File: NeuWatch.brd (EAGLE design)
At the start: 43.2 x 40.6 mm, 68 parts, among them IC1 SAMD21G18A-AUT, IC3 TPS2115, IC4 SIP32401A, IC5 MC74VHC1G14DFT, T1 846, T2 2N7002_ALT, Y1 32,768Khz

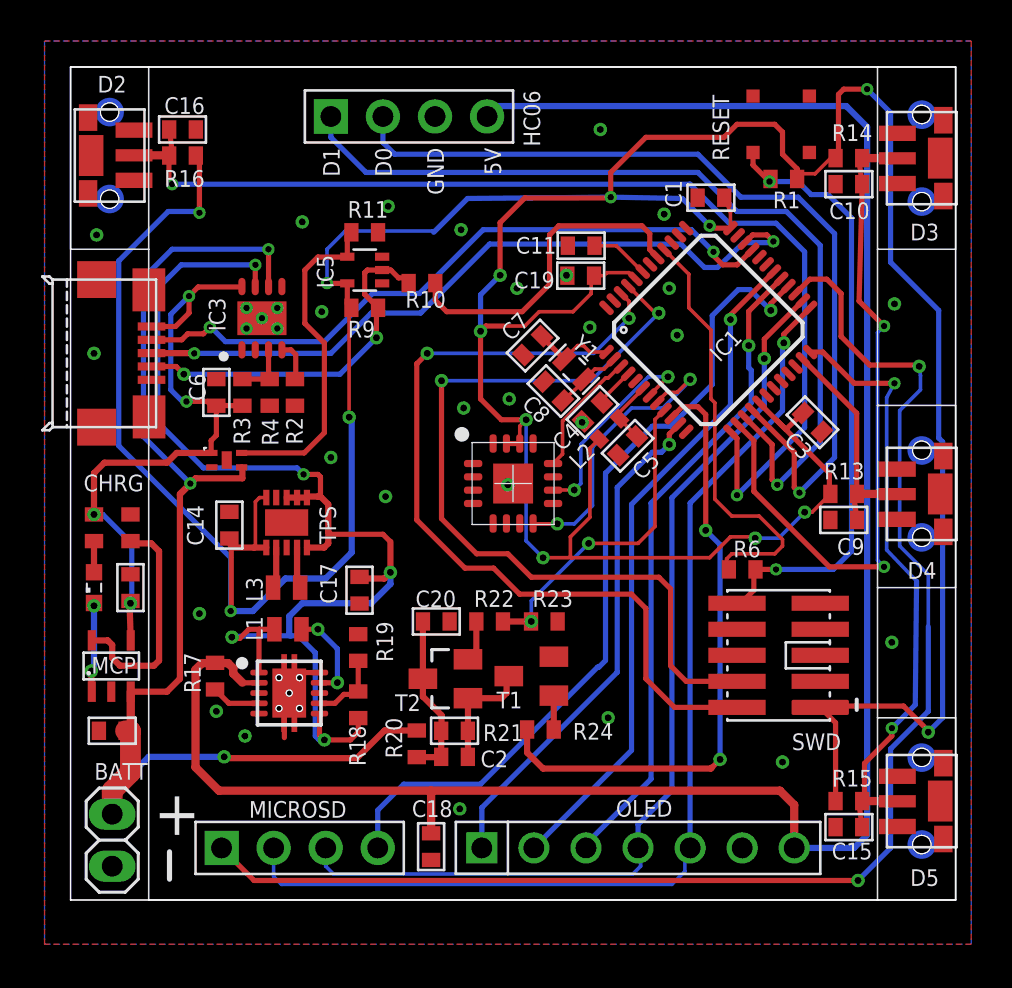
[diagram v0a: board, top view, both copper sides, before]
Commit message: removed boost and others
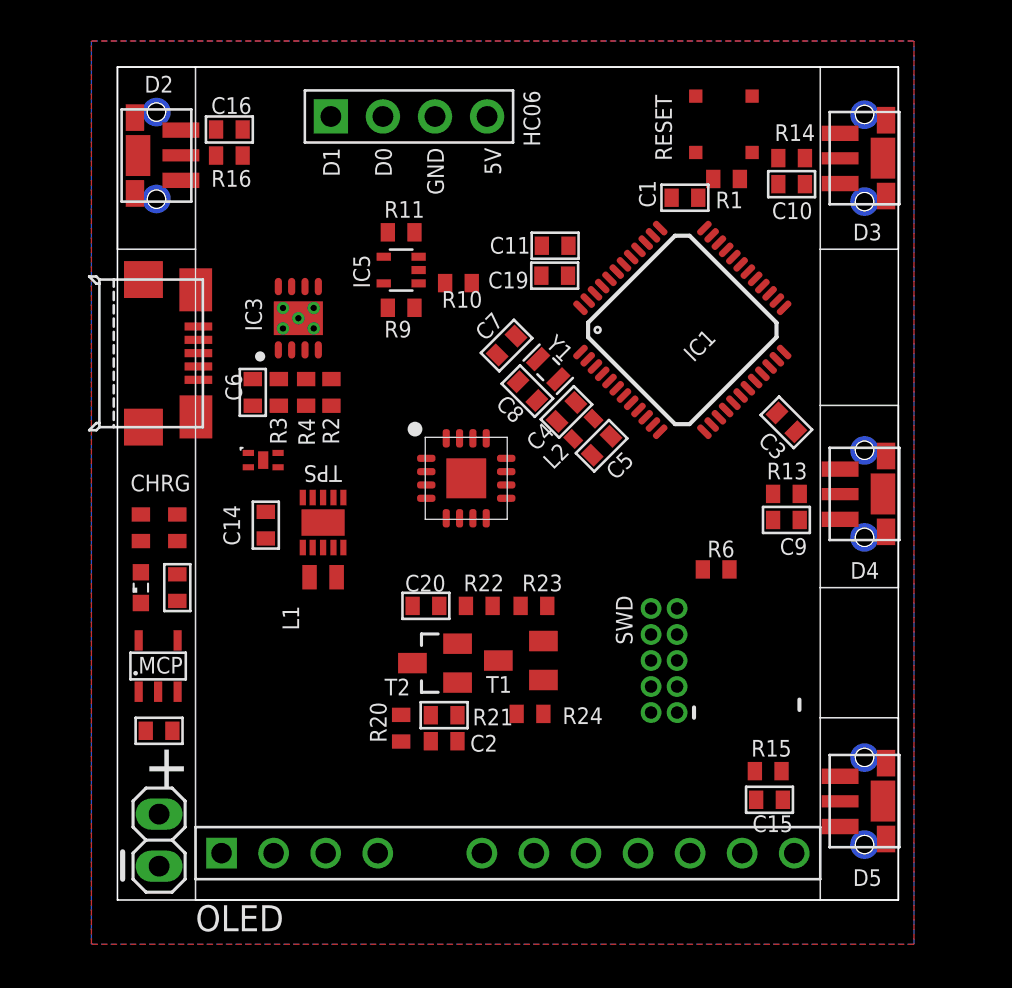
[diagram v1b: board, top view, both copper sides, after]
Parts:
- removed BOOST: TPS6102X, AtomTech:DRC
- removed C17: 10 uF, AtomTech:C0402
- removed C18: 47uf, AtomTech:C0402
- removed L3: 6.8 uH, Bourns_By_element14_Batch_1:INDC1610X12N
- removed MICROSD: 1X4, AtomTech:1B4
- removed R17, R18, R19: 100K, adafruit:R0402
- OLED: value 1X7 -> 1.5-OLED; device AtomTech:1X7 -> AtomTech:1.5OLED
- SWD: value SWD -> PINHEAD-2x5-P1.27; device AtomTech:PARTS_CC-P05 -> Neutrino-:ARDUINO-NEUTRINO-082_CONNETTORI_PINHEAD-2X5-P127
- moved OLED 12.7 mm to (7.49, 2.29)
- moved SWD 5.59 mm to (29.1, 11.7), turned to 180 degrees
- moved R15 4.20 mm to (34.2, 6.29)
- moved C15 4.10 mm to (34.2, 4.89)
- moved C10 2.79 mm to (35.3, 34.9)
- moved R14 2.79 mm to (35.3, 36.2)
- moved RESET 2.79 mm to (32.0, 37.8)
- moved C9 2.79 mm to (35.1, 18.5)
- moved D3 2.79 mm to (38.9, 36.2)
- moved D4 2.79 mm to (38.9, 19.8)
- moved D5 2.79 mm to (38.9, 4.83)
- moved R1 2.79 mm to (32.1, 35.2)
- moved R13 2.79 mm to (35.1, 19.8)
- moved U$1 2.30 mm to (19.4, 20.6)
- moved BATT 2.29 mm to (4.45, 2.92)
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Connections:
- removed net 5V: BOOST.2, C18.1, HC06.P$4, OLED.P$7, R17.2
- removed net LBI: BOOST.7, R18.1, R19.2
- removed net LBO: BOOST.4, R17.1
- removed net SW: BOOST.9, L3.2
- net D6: now also OLED.P$9; no longer OLED.P$3
- net D7: now also OLED.P$5; no longer OLED.P$2
- net D8: now also OLED.P$6; no longer OLED.P$1
- net GND: now also OLED.P$10; no longer BOOST.10, BOOST.5, BOOST.8, BOOST.EXP, C17.2, C18.2, OLED.P$6, R19.1
- net MISO/D12: now also OLED.P$4; no longer MICROSD.P$4
- net MOSI/D11: now also OLED.P$2, OLED.P$7; no longer MICROSD.P$2, OLED.P$5
- net SCK/D13: now also OLED.P$3, OLED.P$8; no longer MICROSD.P$3, OLED.P$4
- net SS/D10: now also OLED.P$1; no longer MICROSD.P$1
- net VIN: now also HC06.P$4, OLED.P$11
- net VMAIN: no longer BOOST.1, BOOST.6, C17.1, L3.1, R18.2
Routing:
- net 3.3V: track 211.1 -> 0.00 mm, vias 14 -> 0
- net 5V: track 100.2 -> 0.00 mm
- net SS/D10: track 68.5 -> 0.00 mm, vias 2 -> 0
- net VIN: track 59.8 -> 0.00 mm, vias 3 -> 0
- net VMAIN: track 58.9 -> 0.00 mm, vias 5 -> 0
- net D2: track 53.2 -> 0.00 mm, vias 2 -> 0
- net MOSI/D11: track 51.9 -> 0.00 mm, vias 1 -> 0
- net SCK/D13: track 47.5 -> 0.00 mm, vias 1 -> 0
- net D1: track 43.6 -> 0.00 mm, vias 1 -> 0
- net D0: track 43.5 -> 0.00 mm, vias 1 -> 0
- net PA31_SWDIO: track 41.7 -> 0.00 mm, vias 2 -> 0
- net MISO/D12: track 40.8 -> 0.00 mm, vias 1 -> 0
- net PA30_SWCLK: track 40.6 -> 0.00 mm, vias 2 -> 0
- net TARGET_USB_P: track 35.2 -> 0.00 mm, vias 2 -> 0
- net D3: track 34.0 -> 0.00 mm, vias 2 -> 0
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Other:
- board size 43.2 x 40.6 mm -> 38.1 x 40.6 mm

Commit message: pinout fixed
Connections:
- net D6: now also OLED.P$5; no longer OLED.P$9
- net D7: now also OLED.P$6; no longer OLED.P$5
- net D8: now also OLED.P$7; no longer OLED.P$6
- net MOSI/D11: now also OLED.P$9; no longer OLED.P$7
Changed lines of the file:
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@@
 <signal name="MOSI/D11">
 <contactref element="IC1" pad="25"/>
-<contactref element="OLED" pad="P$7"/>
+<contactref element="OLED" pad="P$9"/>
 <contactref element="OLED" pad="P$2"/>
-<wire x1="25.273" y1="2.286" x2="34.939425" y2="28.8913375" width="0" layer="19" extent="1-1"/>
-<wire x1="10.033" y1="2.286" x2="25.273" y2="2.286" width="0" layer="19" extent="1-1"/>
+<wire x1="30.353" y1="2.286" x2="34.939425" y2="28.8913375" width="0" layer="19" extent="1-1"/>
+<wire x1="10.033" y1="2.286" x2="30.353" y2="2.286" width="0" layer="19" extent="1-1"/>
 </signal>
 <signal name="SS/D10">
@@
 <signal name="D6">
 <contactref element="IC1" pad="29"/>
-<contactref element="OLED" pad="P$9"/>
-<wire x1="30.353" y1="2.286" x2="33.525209375" y2="30.30555" width="0" layer="19" extent="1-1"/>
+<contactref element="OLED" pad="P$5"/>
+<wire x1="20.193" y1="2.286" x2="33.525209375" y2="30.30555" width="0" layer="19" extent="1-1"/>
 </signal>
 <signal name="TARGET_USB_N">
@@
 <signal name="D7">
 <contactref element="IC1" pad="30"/>
-<contactref element="OLED" pad="P$5"/>
-<wire x1="20.193" y1="2.286" x2="33.17165625" y2="30.659103125" width="0" layer="19" extent="1-1"/>
+<contactref element="OLED" pad="P$6"/>
+<wire x1="22.733" y1="2.286" x2="33.17165625" y2="30.659103125" width="0" layer="19" extent="1-1"/>
 </signal>
 <signal name="D8">
 <contactref element="IC1" pad="11"/>
-<contactref element="OLED" pad="P$6"/>
-<wire x1="22.733" y1="2.286" x2="28.54010625" y2="23.199128125" width="0" layer="19" extent="1-1"/>
+<contactref element="OLED" pad="P$7"/>
+<wire x1="25.273" y1="2.286" x2="28.54010625" y2="23.199128125" width="0" layer="19" extent="1-1"/>
 </signal>
 <signal name="D9">

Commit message: high side load
for OLED and UART cutoff
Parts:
- added C17, C18: 470nf, AtomTech:C0402
- added R7: 10, rcl:R0402
- added R8: 4.7k, rcl:R0402
- added U$3: AAT4610B, AtomTech:SOT23-5
- moved C20 3.64 mm to (21.0, 13.6)
- moved R20 3.64 mm to (19.8, 7.62)
- moved R22 3.64 mm to (23.6, 13.6)
- moved R23 3.64 mm to (26.3, 13.6)
- moved R24 3.64 mm to (26.1, 8.32)
- moved T1 3.64 mm to (25.7, 10.9)
- moved T2 3.64 mm to (21.5, 10.8)
- moved C2 3.64 mm to (21.9, 8.26)
- moved R21 3.64 mm to (21.9, 6.99)
- moved SWD 3.30 mm to (32.4, 11.8)
- moved R6 0.77 mm to (31.8, 16.9), turned to 270 degrees
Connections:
- new net N$10: R7.2, U$3.4
- new net N$11: R8.2, U$3.3
- new net VCBATT: C17.1, HC06.P$4, OLED.P$11, U$3.1
- net D9: now also R7.1
- net GND: now also C17.2, C18.2, R8.1, U$3.2
- net VIN: now also C18.1, U$3.5; no longer HC06.P$4, OLED.P$11

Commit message: fixes
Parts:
- L1: value 1.5 uH -> 120 nH
- RESET: device parts:PTS540 -> AtomTech:PTS540
- moved R10 10.3 mm to (9.14, 33.0), turned to 180 degrees
- moved R7 7.38 mm to (8.26, 12.6), turned to 270 degrees
- moved R11 7.22 mm to (9.14, 31.3), turned to 0 degrees
- moved R1 6.77 mm to (25.9, 37.8), turned to 90 degrees
- moved IC4 6.37 mm to (9.02, 15.1)
- moved R8 5.67 mm to (10.9, 12.6), turned to 270 degrees
- moved IC5 4.78 mm to (11.7, 32.1), turned to 180 degrees
- moved C17 4.56 mm to (11.0, 5.71), turned to 270 degrees
- moved R9 4.16 mm to (13.7, 32.1), turned to 270 degrees
- moved U$1 2.05 mm to (21.5, 20.3)
- moved RESET 1.90 mm to (30.1, 37.8)
- moved U$3 1.78 mm to (10.9, 9.27), turned to 90 degrees
- moved C18 1.42 mm to (8.51, 5.71), turned to 270 degrees
- moved C6 1.20 mm to (8.64, 23.6)
- moved IC3 1.20 mm to (10.9, 27.2)
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
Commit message: redesign
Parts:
- moved RESET 26.8 mm to (38.1, 12.3), turned to 270 degrees
- moved R1 22.7 mm to (33.3, 16.4), turned to 0 degrees
- moved R23 11.0 mm to (15.4, 12.3), turned to 270 degrees
- moved R22 9.15 mm to (15.4, 9.65), turned to 270 degrees
- moved C20 8.64 mm to (15.4, 7.05), turned to 90 degrees
- moved T1 7.66 mm to (18.0, 11.7), turned to 180 degrees
- moved R24 6.66 mm to (20.6, 12.1), turned to 270 degrees
- moved T2 4.67 mm to (18.2, 7.49), turned to 180 degrees
- moved C11 2.73 mm to (25.6, 33.9), turned to 135 degrees
- moved C19 2.51 mm to (24.6, 32.8), turned to 135 degrees
- moved R20 2.34 mm to (21.3, 5.84), turned to 180 degrees
- moved C9 2.05 mm to (35.8, 20.4), turned to 90 degrees
- moved C10 1.94 mm to (35.7, 36.8), turned to 90 degrees
- moved C6 1.78 mm to (10.4, 23.7)
- moved IC3 1.78 mm to (12.6, 27.4)
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
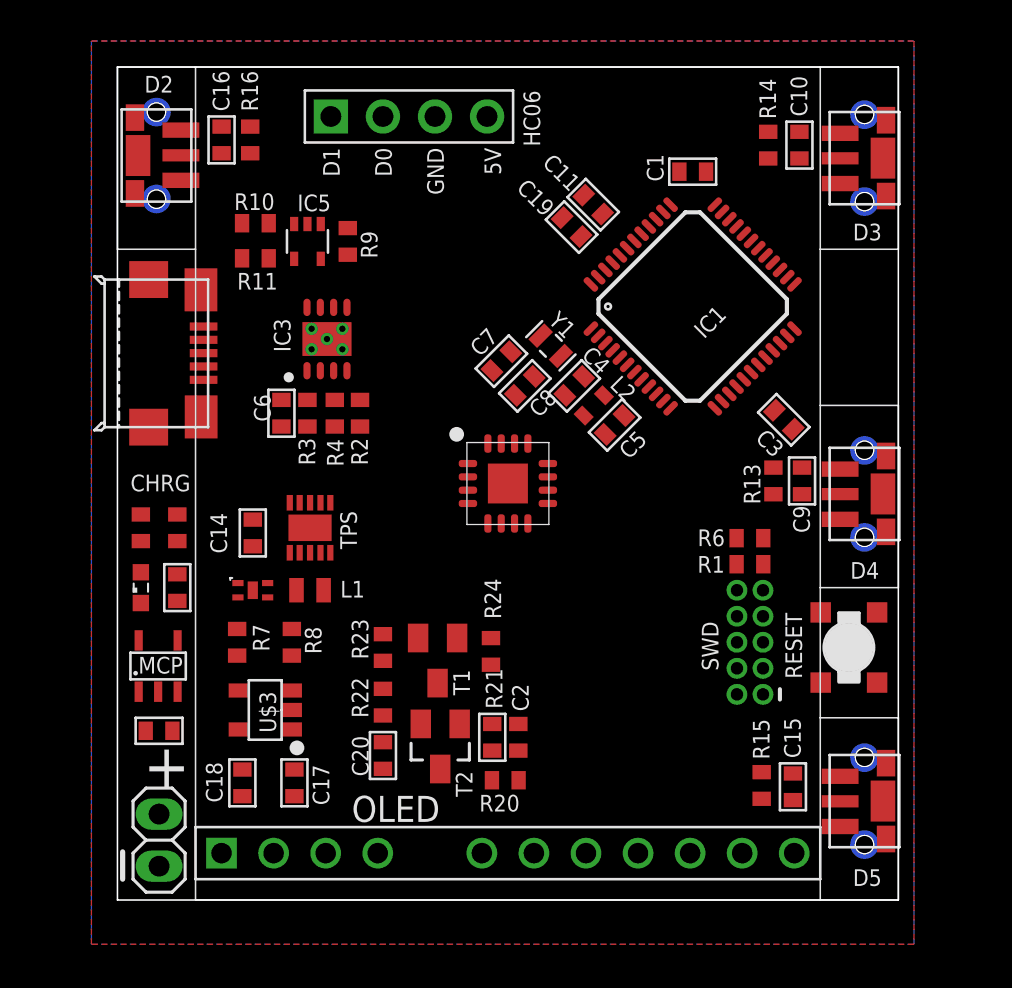
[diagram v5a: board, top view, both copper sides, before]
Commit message: vin control
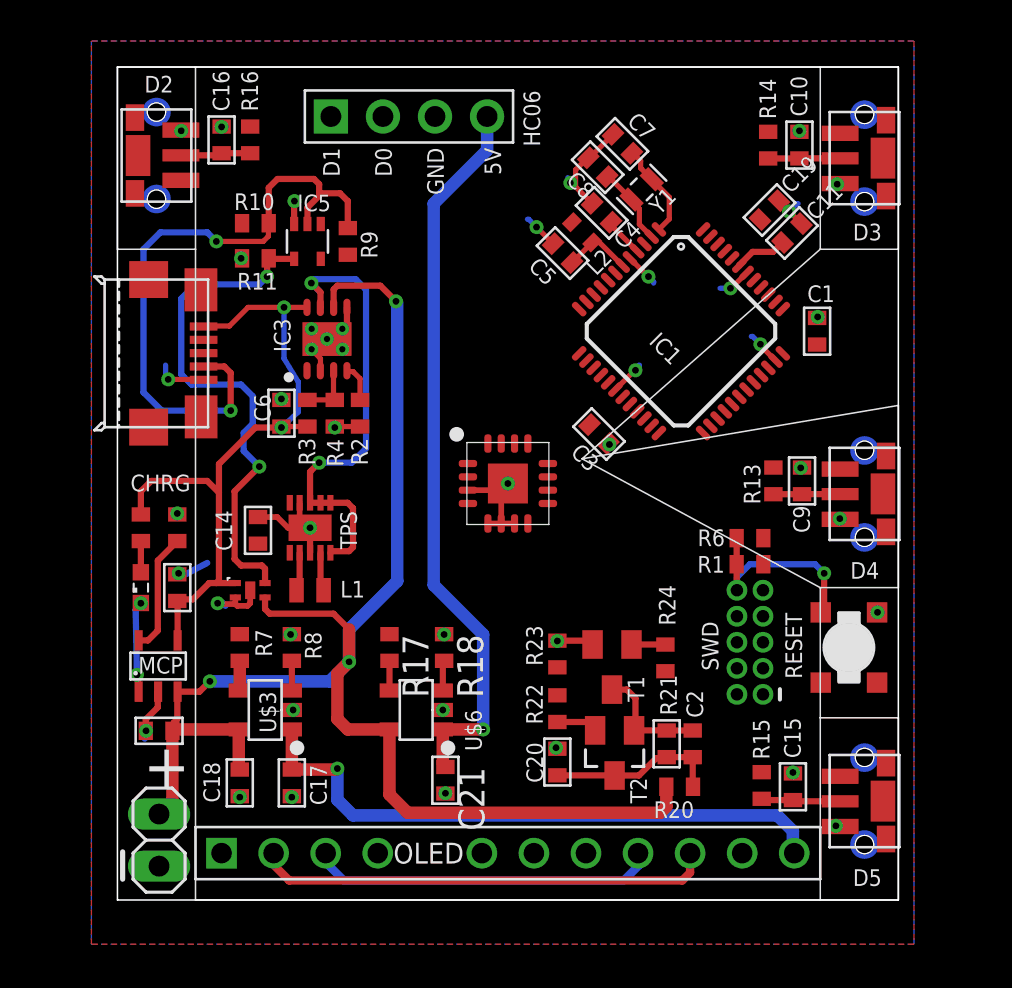
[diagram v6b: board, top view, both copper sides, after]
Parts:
- added C21: 470nf, AtomTech:C0402
- added R17: 10, rcl:R0402
- added R18: 4.7k, rcl:R0402
- added U$6: AAT4610B, AtomTech:SOT23-5
- moved C7 12.1 mm to (27.1, 36.9), turned to 315 degrees
- moved C8 11.2 mm to (25.8, 35.8), turned to 315 degrees
- moved C1 9.87 mm to (36.5, 27.7), turned to 90 degrees
- moved C11 9.80 mm to (35.3, 32.5), turned to 45 degrees
- moved C19 9.69 mm to (34.2, 33.7), turned to 45 degrees
- moved C3 9.04 mm to (25.9, 22.7)
- moved Y1 8.83 mm to (28.0, 34.7), turned to 45 degrees
- moved C5 8.76 mm to (24.1, 31.6), turned to 135 degrees
- moved C4 8.55 mm to (26.0, 33.5), turned to 135 degrees
- moved C2 8.51 mm to (29.2, 7.62)
- moved C20 8.51 mm to (23.9, 6.73)
- moved R20 8.51 mm to (29.8, 5.52)
- moved R21 8.51 mm to (30.5, 7.62)
- moved R22 8.51 mm to (23.9, 9.33)
- moved R23 8.51 mm to (23.9, 12.0)
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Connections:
- removed net VCBATT: C17.1, HC06.P$4, OLED.P$11, U$3.1
- new net N$12: R17.2, U$6.4
- new net N$13: R18.2, U$6.3
- new net VCC_HC05: C21.1, HC06.P$4, U$6.1
- new net VCC_OLED: C17.1, OLED.P$11, U$3.1
- net GND: now also C21.2, R18.1, U$6.2
- net PA04_AIN4: now also R17.1; no longer R22.1, R23.2
- net PB02_AIN10: now also R22.1, R23.2
- net VIN: now also U$6.5
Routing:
- net VIN: track 0.00 -> 74.0 mm, vias 0 -> 3
- net GND: track 0.00 -> 44.7 mm, vias 0 -> 38
- net VCC_HC05: track 0.00 -> 35.8 mm, vias 0 -> 1
- net VBUS: track 0.00 -> 33.4 mm, vias 0 -> 2
- net N$7: track 0.00 -> 31.8 mm, vias 0 -> 2
- net VCC_OLED: track 0.00 -> 29.7 mm, vias 0 -> 1
- net IC4_EN: track 0.00 -> 25.8 mm, vias 0 -> 2
- net VMAIN: track 0.00 -> 22.7 mm, vias 0 -> 2
- net MOSI/D11: track 0.00 -> 22.4 mm
- net SCK/D13: track 0.00 -> 17.0 mm
- net RESET: track 0.00 -> 9.86 mm, vias 0 -> 1
- net N$9: track 0.00 -> 8.43 mm
- net N$3: track 0.00 -> 5.89 mm
- net N$5: track 0.00 -> 5.78 mm
- net PA00_XIN32: track 0.00 -> 4.72 mm
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- added copper zone on layer 1, net 3.3V
- removed copper zone on layer 1, net GND

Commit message: traced
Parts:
- moved SWD 26.1 mm to (30.6, 38.5), turned to 270 degrees
- moved RESET 3.37 mm to (34.7, 12.4)
- moved R1 2.73 mm to (36.0, 16.4), turned to 90 degrees
- moved R6 1.58 mm to (34.3, 16.4), turned to 270 degrees
- moved R14 1.17 mm to (35.2, 36.3), turned to 180 degrees
- moved C5 1.08 mm to (23.4, 32.3)
- moved C10 1.02 mm to (35.2, 37.7), turned to 180 degrees
- moved C3 0.89 mm to (26.8, 22.7)
- moved C7 0.18 mm to (26.9, 36.8)
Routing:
- net D8: track 0.00 -> 48.0 mm, vias 0 -> 1
- net D1: track 0.00 -> 44.2 mm, vias 0 -> 1
- net PB02_AIN10: track 0.00 -> 44.1 mm, vias 0 -> 3
- net SS/D10: track 0.00 -> 43.9 mm, vias 0 -> 1
- net PA28_USB_HOST_EN: track 0.00 -> 40.9 mm, vias 0 -> 2
- net PA05_AIN5: track 0.00 -> 38.1 mm, vias 0 -> 2
- net SCK/D13: track 17.0 -> 53.4 mm, vias 0 -> 2
- net TARGET_USB_P: track 0.00 -> 36.1 mm, vias 0 -> 2
- net D9: track 0.00 -> 35.6 mm, vias 0 -> 2
- net TARGET_USB_N: track 0.00 -> 33.9 mm, vias 0 -> 2
- net D7: track 0.00 -> 33.0 mm, vias 0 -> 1
- net MISO/D12: track 0.00 -> 32.9 mm, vias 0 -> 1
- net D6: track 0.00 -> 31.9 mm, vias 0 -> 1
- net MOSI/D11: track 22.4 -> 52.7 mm, vias 0 -> 2
- net D0: track 0.00 -> 28.6 mm, vias 0 -> 2
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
